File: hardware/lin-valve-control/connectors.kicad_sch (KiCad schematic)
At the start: 7 parts

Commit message: Update lin-master firmware and valve control board
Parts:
- removed J? (x2): Screw_Terminal_01x03, TerminalBlock_TE-Connectivity:TerminalBlock_TE_282834-3_1x03_P2.54mm_Horizontal, symbol Connector:Screw_Terminal_01x03
- added J2, J4: DIN5, SparkFun-Connectors:DIN5-RA-PTH, symbol SparkFun-Connectors:DIN5
- gave numbers to parts that had none: 5
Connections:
- net GND: now also J2.2, J4.2
- net VALVE1+: now also J2.1
- net VALVE1-: now also J2.3
- net VALVE2+: now also J4.1
- net VALVE2-: now also J4.3
- new net VALVE1_CLOSED: J2.5
- new net VALVE1_OPEN: J2.4
- new net VALVE2_CLOSED: J4.5
- new net VALVE2_OPEN: J4.4

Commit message: Updated valve controller board
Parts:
- renumbered J7 to J1, J5 to J2, J1 to J3, J3 to J4, J6 to J5, J4 to J6, J2 to J7
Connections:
- net SCL renamed SCL3V
- net SDA renamed SDA3V
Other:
- company: (none) -> Gavin Hurlbut
- title: (none) -> LINBus Valve Controller
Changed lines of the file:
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@@
 (kicad_sch (version 20211123) (generator eeschema)
   (paper "A4")
+  (title_block
+    (title "LINBus Valve Controller")
+    (date "2023-02-15")
+    (rev "1.0")
+    (company "Gavin Hurlbut")
+  )
   (junction (at 114.3 180.848) (diameter 0) (color 0 0 0 0)
   )
@@
     )
   )
-  (global_label "SCL" (shape bidirectional) (at 114.935 29.337 180) (fields_autoplaced)
-    (effects (font (size 1.27 1.27)) (justify right))
-    (property "Intersheet References" "${INTERSHEET_REFS}" (id 0) (at 109.1032 29.2576 0)
+  (global_label "SCL3V" (shape bidirectional) (at 114.935 29.337 180) (fields_autoplaced)
+    (effects (font (size 1.27 1.27)) (justify right))
+    (property "Intersheet References" "${INTERSHEET_REFS}" (id 0) (at 106.8051 29.2576 0)
       (effects (font (size 1.27 1.27)) (justify right) hide)
     )
@@
     )
   )
-  (global_label "SDA" (shape bidirectional) (at 114.935 31.877 180) (fields_autoplaced)
-    (effects (font (size 1.27 1.27)) (justify right))
-    (property "Intersheet References" "${INTERSHEET_REFS}" (id 0) (at 109.0427 31.7976 0)
+  (global_label "SDA3V" (shape bidirectional) (at 114.935 31.877 180) (fields_autoplaced)
+    (effects (font (size 1.27 1.27)) (justify right))
+    (property "Intersheet References" "${INTERSHEET_REFS}" (id 0) (at 106.7446 31.7976 0)
       (effects (font (size 1.27 1.27)) (justify right) hide)
     )
@@
   (symbol (lib_id "power:GND") (at 114.3 186.182 0) (unit 1)
     (in_bom yes) (on_board yes) (fields_autoplaced)
-    (property "Reference" "#PWR024" (id 0) (at 114.3 192.532 0)
+    (property "Reference" "#PWR07" (id 0) (at 114.3 192.532 0)
       (effects (font (size 1.27 1.27)) hide)
     )
@@
   (symbol (lib_id "Connector:Screw_Terminal_01x04") (at 122.047 175.768 0) (unit 1)
     (in_bom yes) (on_board yes) (fields_autoplaced)
-    (property "Reference" "J7" (id 0) (at 125.222 175.7679 0)
+    (property "Reference" "J1" (id 0) (at 125.222 175.7679 0)
       (effects (font (size 1.27 1.27)) (justify left))
     )
@@
   (symbol (lib_id "SparkFun-Connectors:DIN5") (at 225.425 57.277 180) (unit 1)
     (in_bom yes) (on_board yes) (fields_autoplaced)
-    (property "Reference" "J2" (id 0) (at 225.425 44.45 0)
+    (property "Reference" "J7" (id 0) (at 225.425 44.45 0)
       (effects (font (size 1.143 1.143)))
     )
@@
   (symbol (lib_id "SparkFun-Connectors:I2C_STANDARDQWIIC") (at 122.682 36.957 0) (mirror y) (unit 1)
     (in_bom yes) (on_board yes) (fields_autoplaced)
-    (property "Reference" "J1" (id 0) (at 129.159 31.877 0)
+    (property "Reference" "J3" (id 0) (at 129.159 31.877 0)
       (effects (font (size 1.143 1.143)) (justify right))
     )
@@
   (symbol (lib_id "power:GND") (at 117.094 38.862 0) (unit 1)
     (in_bom yes) (on_board yes) (fields_autoplaced)
-    (property "Reference" "#PWR016" (id 0) (at 117.094 45.212 0)
+    (property "Reference" "#PWR014" (id 0) (at 117.094 45.212 0)
       (effects (font (size 1.27 1.27)) hide)
     )
@@
   (symbol (lib_id "Connector:Screw_Terminal_01x02") (at 122.555 122.301 0) (unit 1)
     (in_bom yes) (on_board yes) (fields_autoplaced)
-    (property "Reference" "J5" (id 0) (at 124.714 122.3009 0)
+    (property "Reference" "J2" (id 0) (at 124.714 122.3009 0)
       (effects (font (size 1.27 1.27)) (justify left))
     )
@@
   (symbol (lib_id "power:+5V") (at 115.189 144.907 0) (unit 1)
     (in_bom yes) (on_board yes) (fields_autoplaced)
-    (property "Reference" "#PWR022" (id 0) (at 115.189 148.717 0)
+    (property "Reference" "#PWR010" (id 0) (at 115.189 148.717 0)
       (effects (font (size 1.27 1.27)) hide)
     )
@@
   (symbol (lib_id "SparkFun-Connectors:DIN5") (at 225.044 112.014 180) (unit 1)
     (in_bom yes) (on_board yes) (fields_autoplaced)
-    (property "Reference" "J4" (id 0) (at 225.044 99.06 0)
+    (property "Reference" "J6" (id 0) (at 225.044 99.06 0)
       (effects (font (size 1.143 1.143)))
     )
@@
   (symbol (lib_id "power:GND") (at 115.316 128.397 0) (unit 1)
     (in_bom yes) (on_board yes) (fields_autoplaced)
-    (property "Reference" "#PWR021" (id 0) (at 115.316 134.747 0)
+    (property "Reference" "#PWR012" (id 0) (at 115.316 134.747 0)
       (effects (font (size 1.27 1.27)) hide)
     )
@@
   (symbol (lib_id "power:+12V") (at 115.189 55.245 0) (unit 1)
     (in_bom yes) (on_board yes) (fields_autoplaced)
-    (property "Reference" "#PWR017" (id 0) (at 115.189 59.055 0)
+    (property "Reference" "#PWR08" (id 0) (at 115.189 59.055 0)
       (effects (font (size 1.27 1.27)) hide)
     )
@@
   (symbol (lib_id "power:GND") (at 225.425 73.533 0) (unit 1)
     (in_bom yes) (on_board yes) (fields_autoplaced)
-    (property "Reference" "#PWR019" (id 0) (at 225.425 79.883 0)
+    (property "Reference" "#PWR016" (id 0) (at 225.425 79.883 0)
       (effects (font (size 1.27 1.27)) hide)
     )
@@
   (symbol (lib_id "power:GND") (at 115.189 155.321 0) (unit 1)
     (in_bom yes) (on_board yes)
-    (property "Reference" "#PWR023" (id 0) (at 115.189 161.671 0)
+    (property "Reference" "#PWR011" (id 0) (at 115.189 161.671 0)
       (effects (font (size 1.27 1.27)) hide)
     )
@@
   (symbol (lib_id "power:GND") (at 115.189 65.659 0) (unit 1)
     (in_bom yes) (on_board yes)
-    (property "Reference" "#PWR018" (id 0) (at 115.189 72.009 0)
+    (property "Reference" "#PWR09" (id 0) (at 115.189 72.009 0)
       (effects (font (size 1.27 1.27)) hide)
     )
@@
   (symbol (lib_id "power:GND") (at 225.044 127.381 0) (unit 1)
     (in_bom yes) (on_board yes)
-    (property "Reference" "#PWR020" (id 0) (at 225.044 133.731 0)
+    (property "Reference" "#PWR015" (id 0) (at 225.044 133.731 0)
       (effects (font (size 1.27 1.27)) hide)
     )
@@
   (symbol (lib_id "Connector:Screw_Terminal_01x03") (at 122.809 150.241 0) (unit 1)
     (in_bom yes) (on_board yes)
-    (property "Reference" "J6" (id 0) (at 124.841 149.1742 0)
+    (property "Reference" "J5" (id 0) (at 124.841 149.1742 0)
       (effects (font (size 1.27 1.27)) (justify left))
     )
@@
   (symbol (lib_id "Connector:Screw_Terminal_01x03") (at 122.809 60.579 0) (unit 1)
     (in_bom yes) (on_board yes)
-    (property "Reference" "J3" (id 0) (at 124.841 59.5122 0)
+    (property "Reference" "J4" (id 0) (at 124.841 59.5122 0)
       (effects (font (size 1.27 1.27)) (justify left))
     )
@@
   (symbol (lib_id "power:+3V3") (at 116.967 25.4 0) (unit 1)
     (in_bom yes) (on_board yes) (fields_autoplaced)
-    (property "Reference" "#PWR015" (id 0) (at 116.967 29.21 0)
-      (effects (font (size 1.27 1.27)) hide)
-    )
+    (property "Reference" "#PWR013" (id 0) (at 116.967 29.21 0)
+      (effects (font (size 1.27 1.27)) hide)
+    )

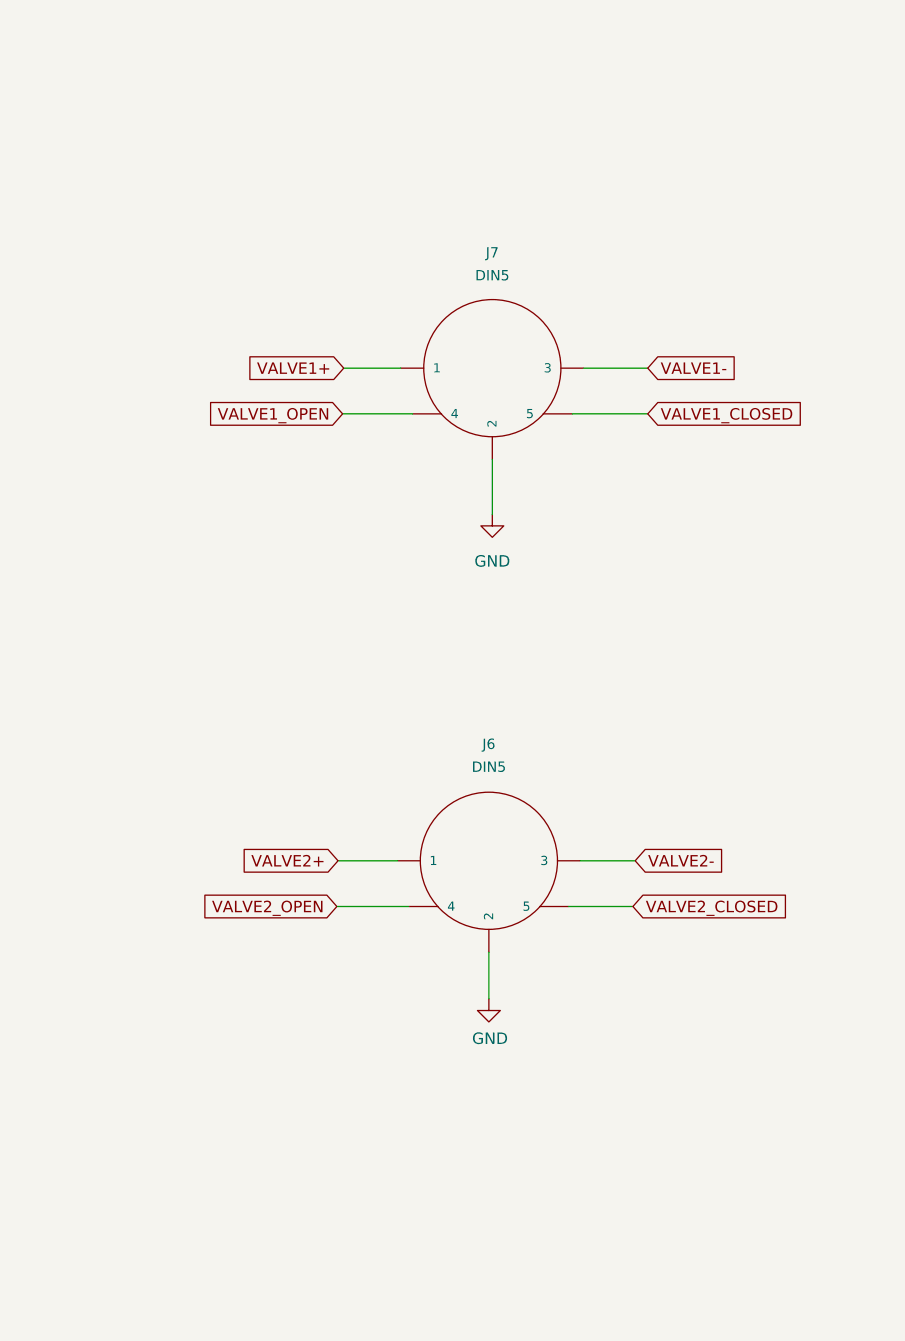
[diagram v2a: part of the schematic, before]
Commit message: Add a connector to attach 20x4 LCD on an I2C backpack
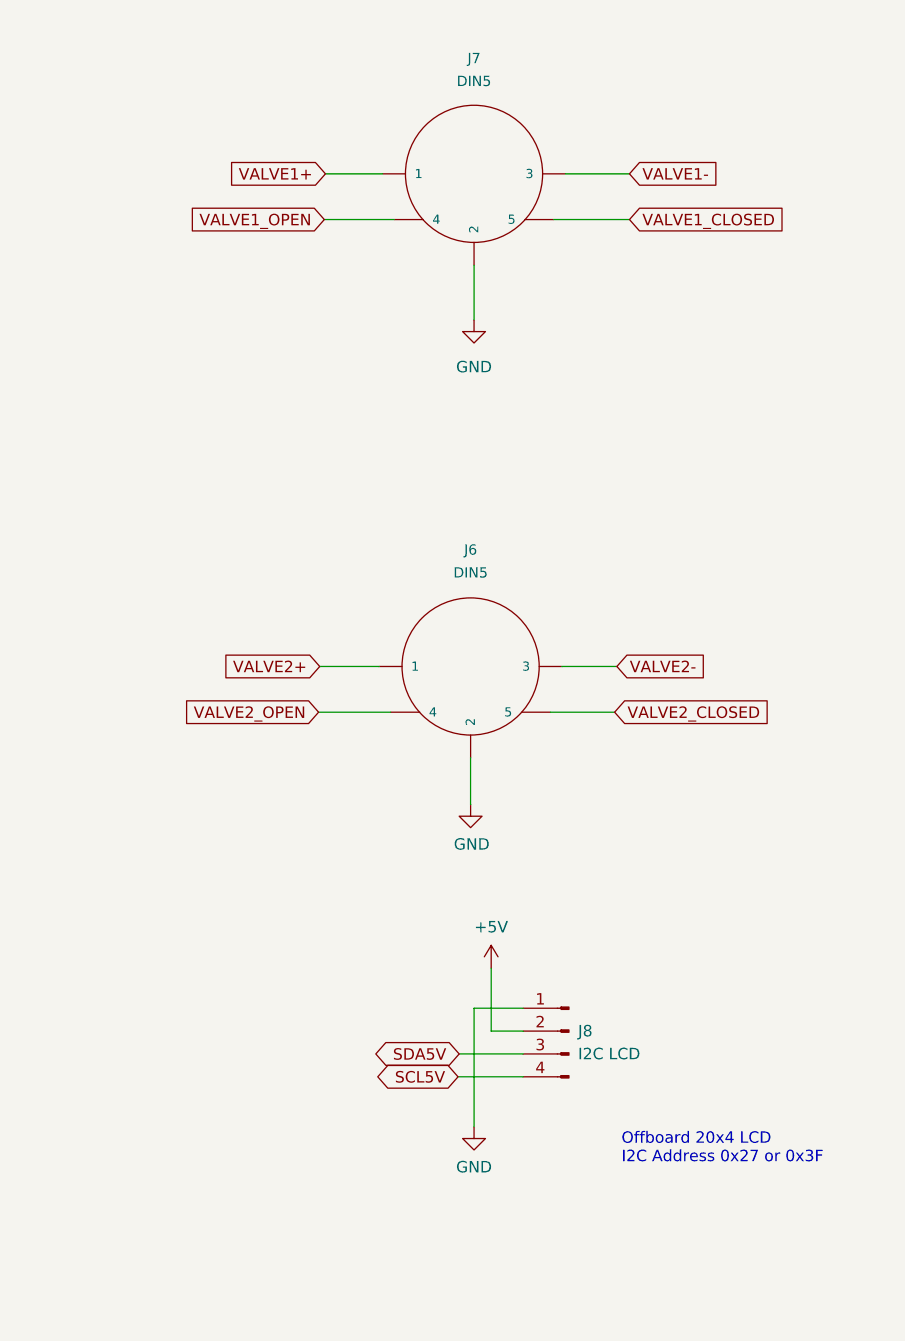
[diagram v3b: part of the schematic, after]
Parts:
- added J8: I2C LCD, Connector_PinHeader_2.54mm:PinHeader_1x04_P2.54mm_Vertical, symbol Connector:Conn_01x04_Male
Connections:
- net +5V: now also J8.2 (Pin_2)
- net GND: now also J8.1 (Pin_1)
- new net SCL5V: J8.4 (Pin_4)
- new net SDA5V: J8.3 (Pin_3)
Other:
- note added: "Offboard 20x4 LCD I2C Address 0x27 or 0x3F"
- moved on the sheet: J6, J7

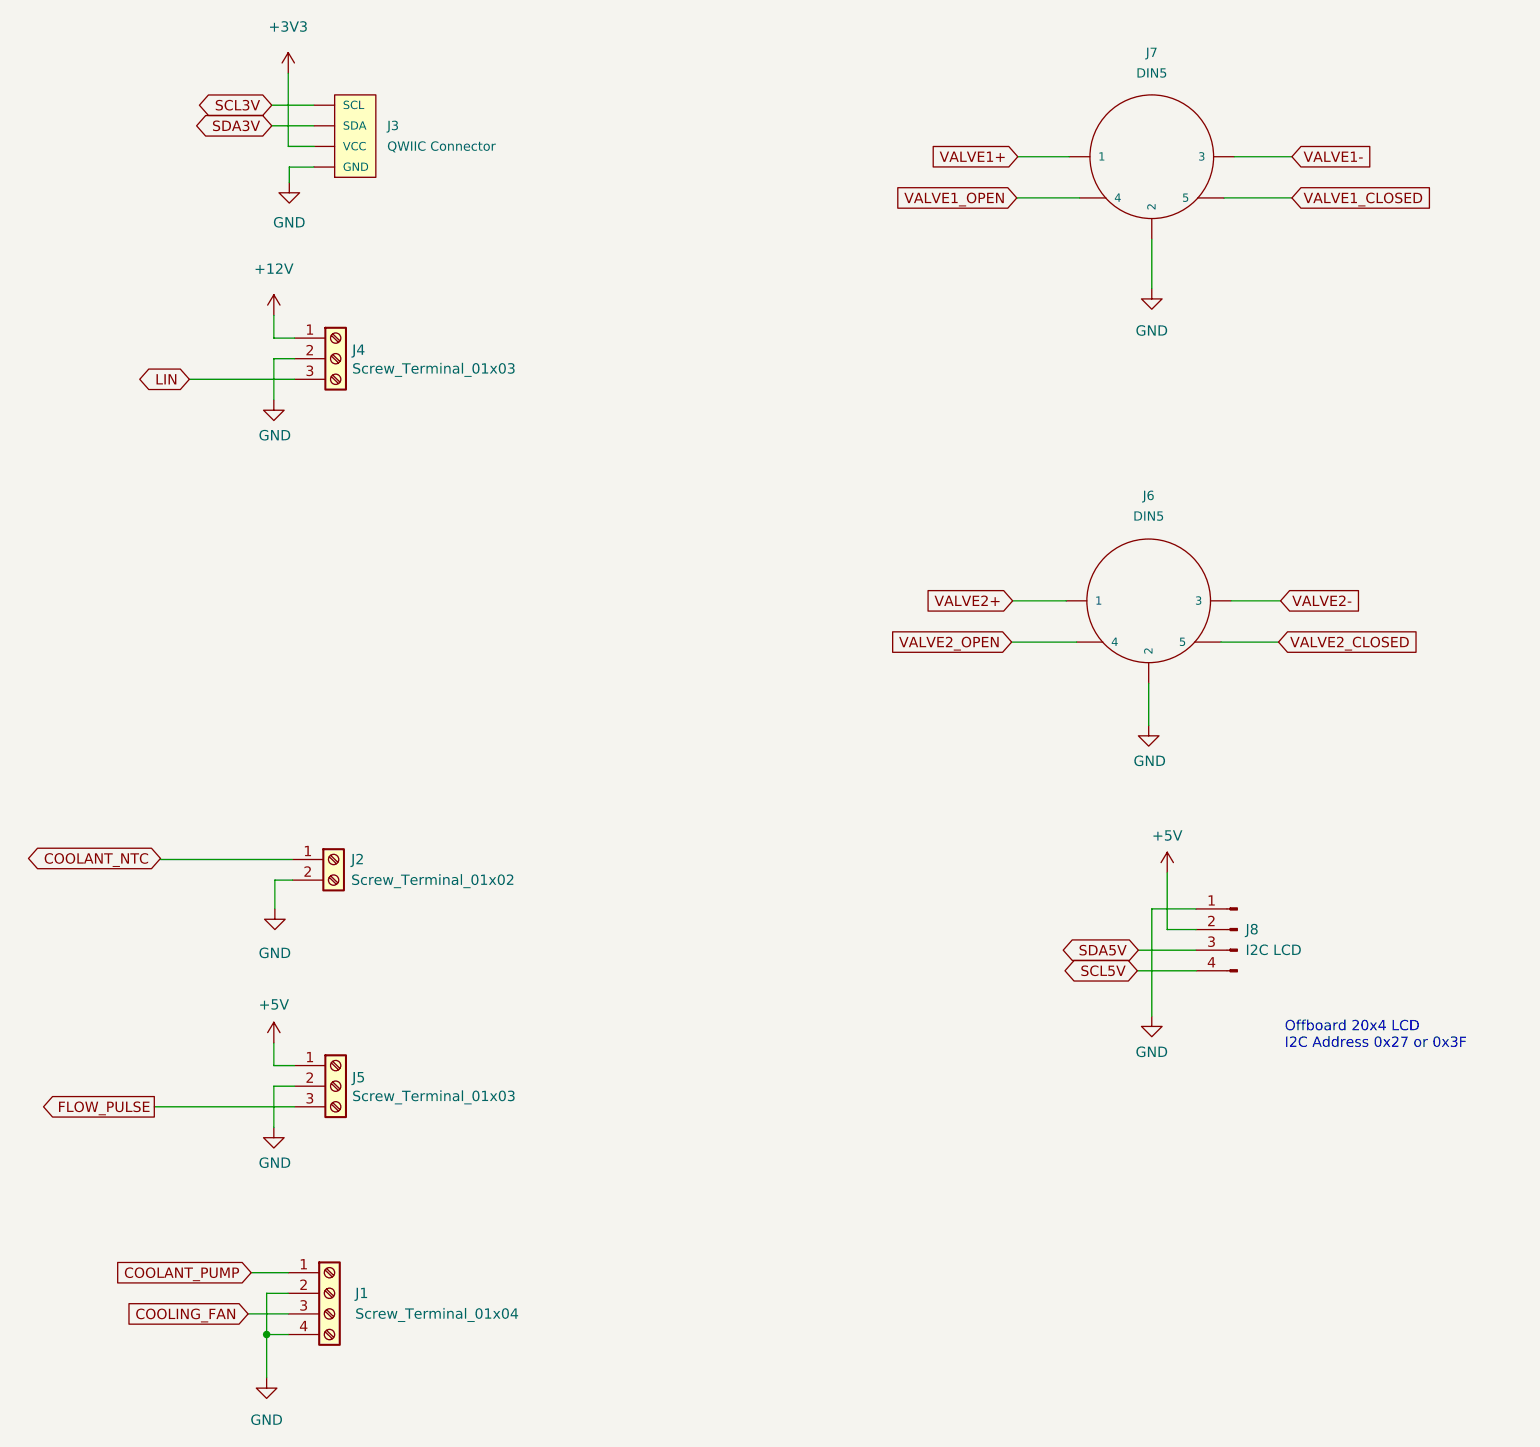
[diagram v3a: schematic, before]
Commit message: Completely redo the valve controller.  One valve only.
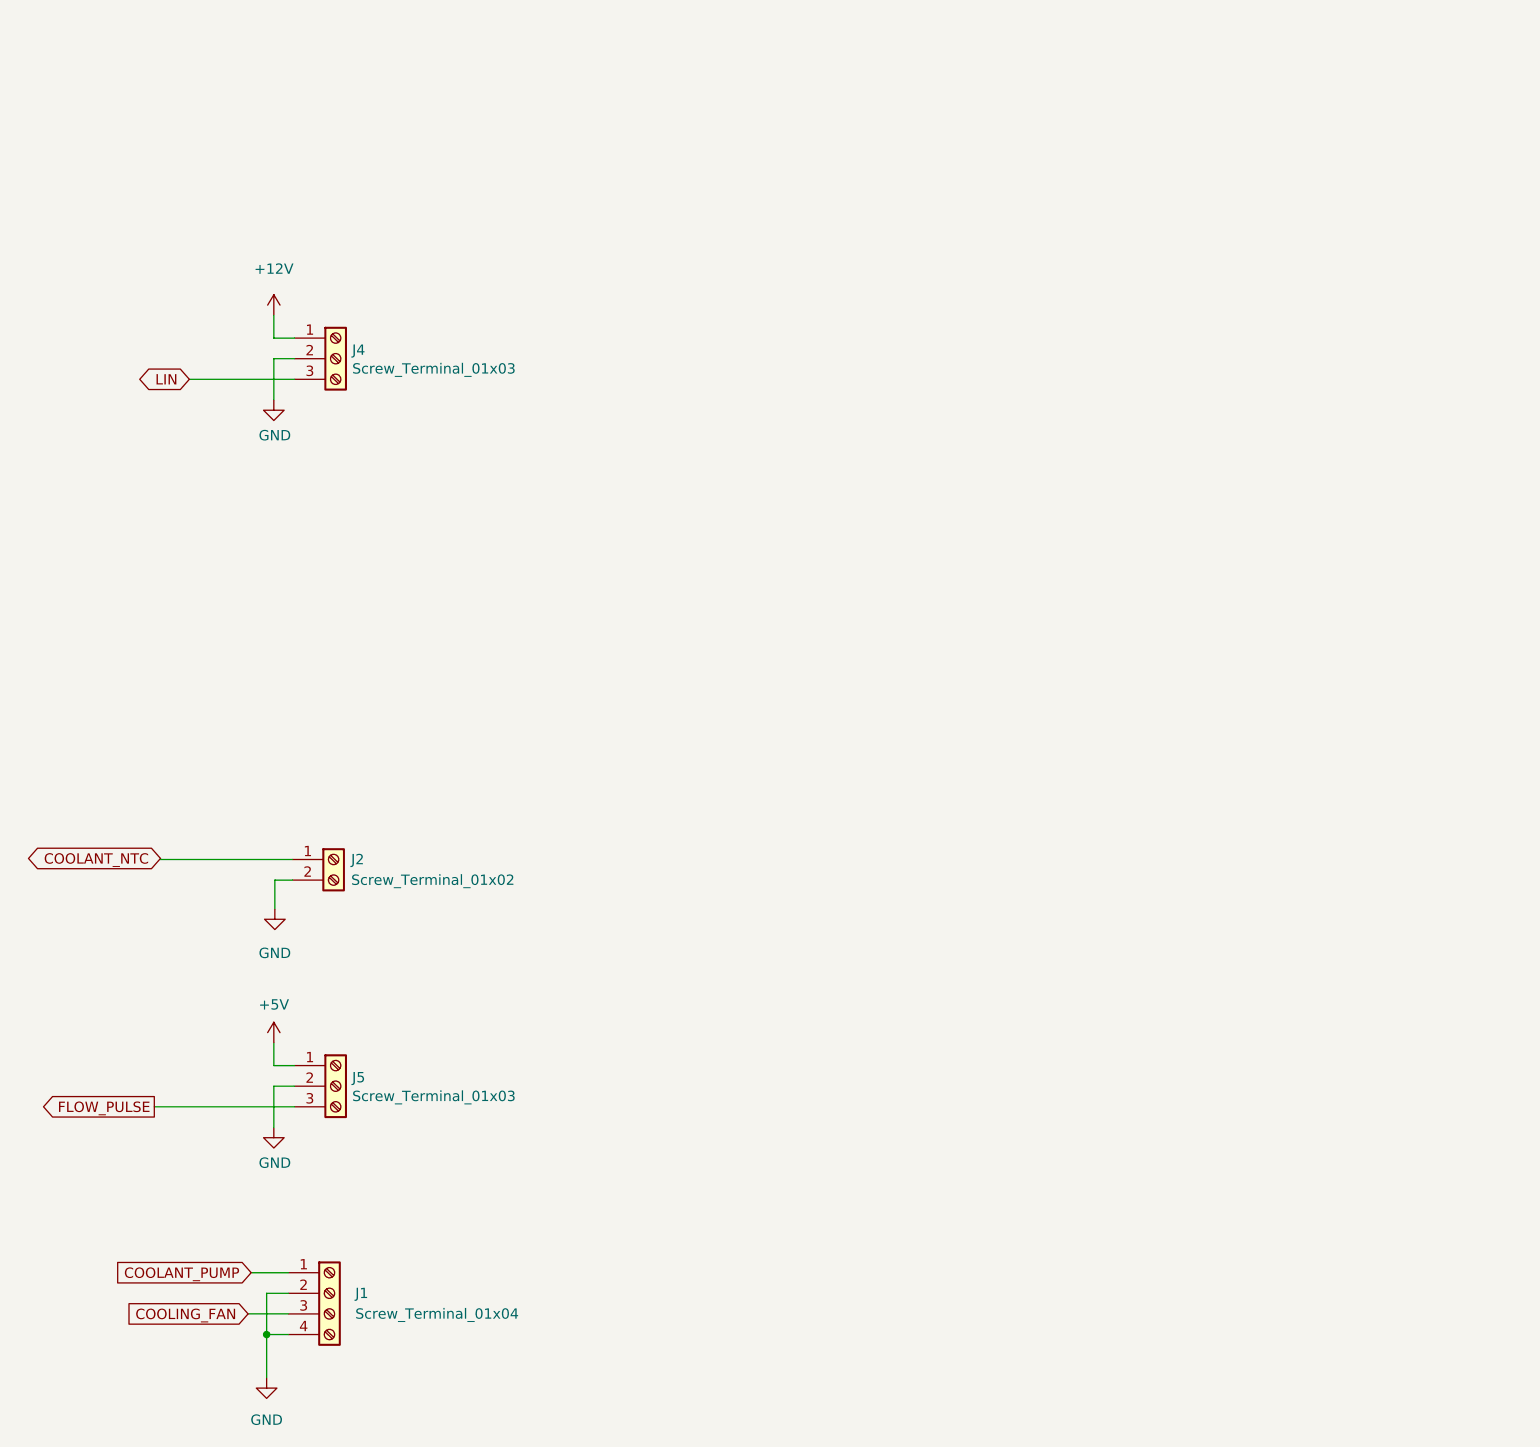
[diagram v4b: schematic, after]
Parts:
- removed J3: QWIIC Connector, SparkFun-Connectors:1X04_1MM_RA, symbol SparkFun-Connectors:I2C_STANDARDQWIIC
- removed J6, J7: DIN5, SparkFun-Connectors:DIN5-RA-PTH, symbol SparkFun-Connectors:DIN5
- removed J8: I2C LCD, Connector_PinHeader_2.54mm:PinHeader_1x04_P2.54mm_Vertical, symbol Connector:Conn_01x04_Male
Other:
- note removed: "Offboard 20x4 LCD I2C Address 0x27 or 0x3F"
